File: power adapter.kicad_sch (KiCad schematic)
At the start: 6 parts, among them J1 Conn_02x05_Odd_Even_MountingP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

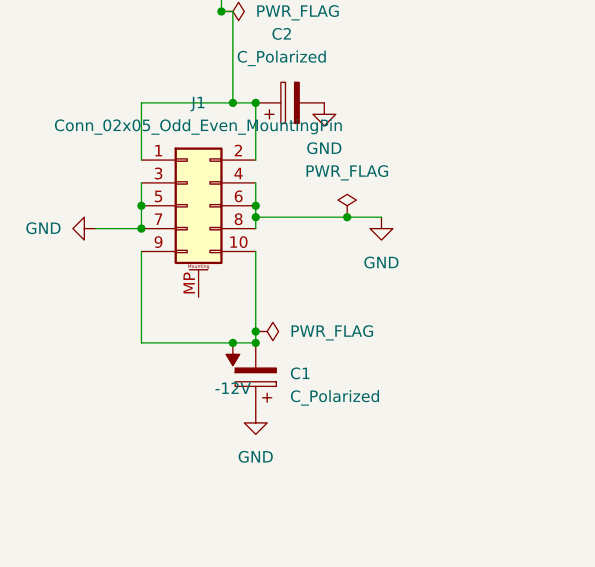
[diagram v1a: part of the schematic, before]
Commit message: added header footprint
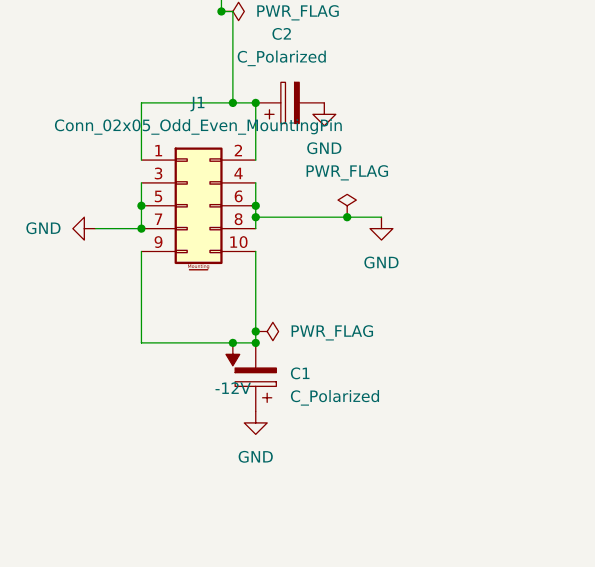
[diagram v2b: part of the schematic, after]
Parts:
- J1: footprint (none) -> Connector_PinHeader_1.00mm:PinHeader_2x05_P1.00mm_Vertical
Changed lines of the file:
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@@
 			)
 		)
-		(property "Footprint" ""
+		(property "Footprint" "Connector_PinHeader_1.00mm:PinHeader_2x05_P1.00mm_Vertical"
 			(at 26.67 48.26 0)
 			(effects
@@
 		(pin "8"
 		)
-		(pin "MP"
-		)
 		(pin "7"

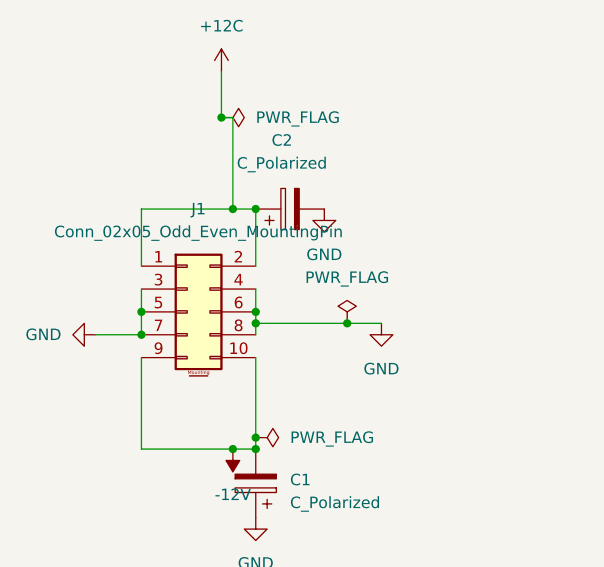
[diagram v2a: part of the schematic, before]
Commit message: fixed header symbol
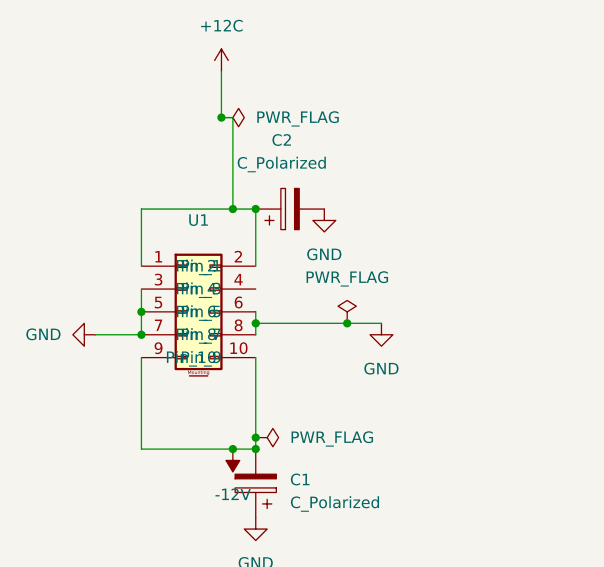
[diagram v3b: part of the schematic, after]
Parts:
- removed J1: Conn_02x05_Odd_Even_MountingPin, Connector_PinHeader_1.00mm:PinHeader_2x05_P1.00mm_Vertical, symbol Connector_Generic_MountingPin:Conn_02x05_Odd_Even_MountingPin
- added U1: ~, symbol adapterlib:header2x5
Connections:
- net +12C: now also U1.1 (Pin_1), U1.2 (Pin_2)
- net -12V: now also U1.10 (Pin_10), U1.9 (Pin_9)
- net GND: now also U1.3 (Pin_3), U1.5 (Pin_5), U1.6 (Pin_6), U1.7 (Pin_7), U1.8 (Pin_8)

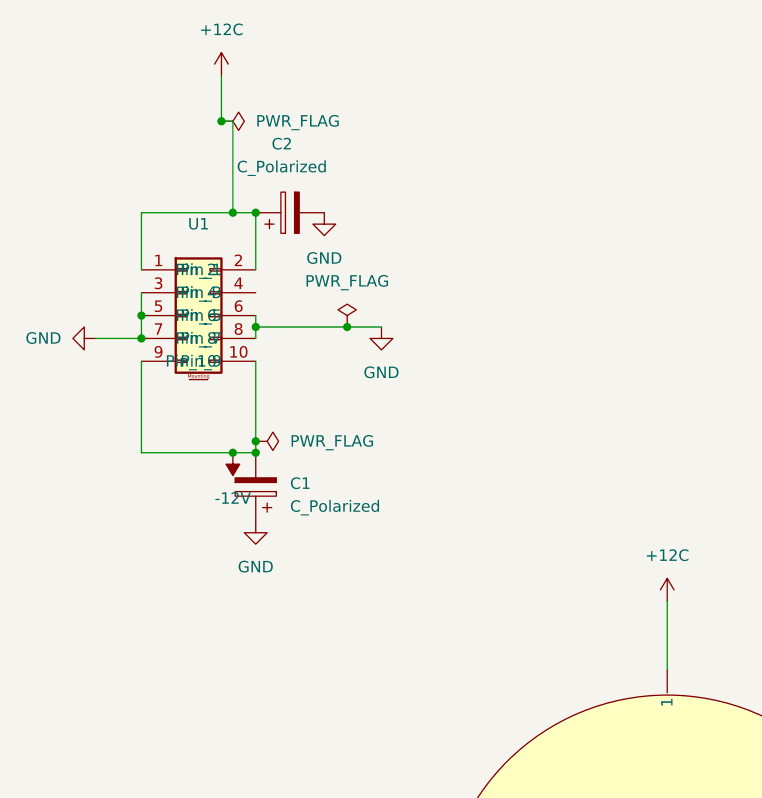
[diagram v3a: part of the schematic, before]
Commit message: added esp32lib to project
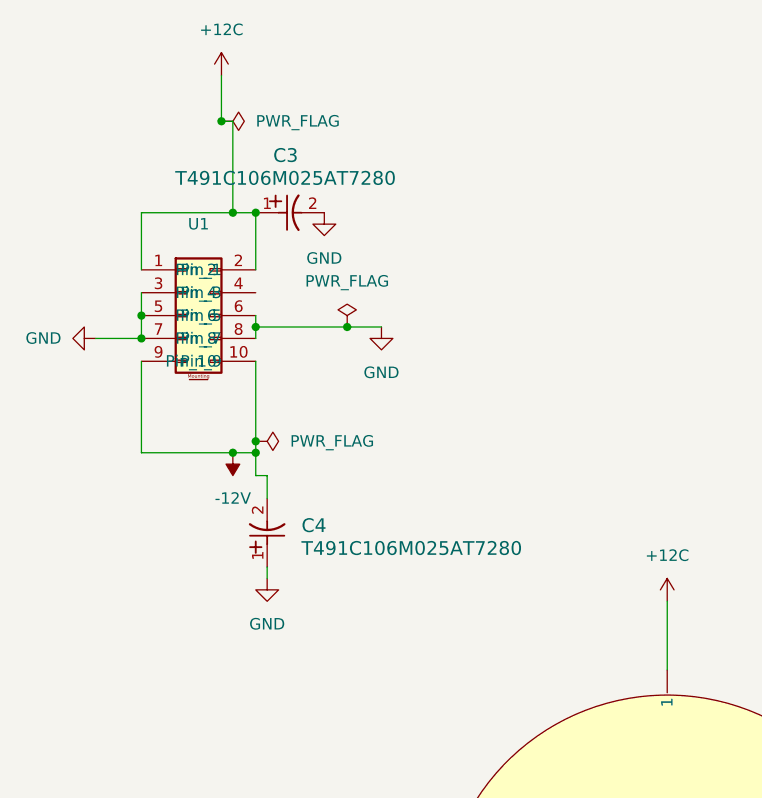
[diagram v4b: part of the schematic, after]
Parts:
- removed C1, C2: C_Polarized, symbol Device:C_Polarized
- added C3, C4: T491C106M025AT7280, customfootprints:10uFtantcap, symbol esp32lib:T491C106M025AT7280
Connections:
- net +12C: now also C3.1
- net -12V: now also C4.2
- net GND: now also C3.2, C4.1
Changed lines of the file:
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@@
 	(paper "A4")
+	(junction
+		(at 44.45 49.53)
+		(diameter 0)
+		(color 0 0 0 0)
+	)
+	(junction
+		(at 21.59 48.26)
+		(diameter 0)
+		(color 0 0 0 0)
+	)
+	(junction
+		(at 30.48 26.67)
+		(diameter 0)
+		(color 0 0 0 0)
+	)
 	(junction
 		(at 34.29 36.83)
@@
 	)
 	(junction
-		(at 44.45 49.53)
-		(diameter 0)
-		(color 0 0 0 0)
-	)
-	(junction
-		(at 21.59 48.26)
-		(diameter 0)
-		(color 0 0 0 0)
-	)
-	(junction
-		(at 30.48 26.67)
-		(diameter 0)
-		(color 0 0 0 0)
-	)
-	(junction
 		(at 21.59 50.8)
 		(diameter 0)
@@
 	)
 	(junction
-		(at 34.29 63.5)
-		(diameter 0)
-		(color 0 0 0 0)
-	)
-	(junction
 		(at 34.29 62.23)
 		(diameter 0)
@@
 	)
 	(junction
+		(at 34.29 63.5)
+		(diameter 0)
+		(color 0 0 0 0)
+	)
+	(junction
 		(at 31.75 63.5)
 		(diameter 0)
@@
 	(wire
 		(pts
+			(xy 34.29 66.04) (xy 34.29 63.5)
+		)
+		(stroke
+			(width 0)
+			(type default)
+		)
+	)
+	(wire
+		(pts
 			(xy 21.59 43.18) (xy 21.59 36.83)
 		)
@@
 	(wire
 		(pts
+			(xy 35.56 77.47) (xy 35.56 76.2)
+		)
+		(stroke
+			(width 0)
+			(type default)
+		)
+	)
+	(wire
+		(pts
 			(xy 34.29 49.53) (xy 34.29 50.8)
 		)
@@
 	(wire
 		(pts
+			(xy 35.56 68.58) (xy 35.56 66.04)
+		)
+		(stroke
+			(width 0)
+			(type default)
+		)
+	)
+	(wire
+		(pts
 			(xy 34.29 48.26) (xy 34.29 49.53)
 		)
@@
 		(pts
 			(xy 140.97 143.51) (xy 148.59 143.51)
+		)
+		(stroke
+			(width 0)
+			(type default)
+		)
+	)
+	(wire
+		(pts
+			(xy 35.56 66.04) (xy 34.29 66.04)
 		)
 		(stroke
@@
 	)
 	(symbol
-		(lib_id "Device:C_Polarized")
-		(at 34.29 67.31 180)
-		(unit 1)
-		(exclude_from_sim no)
-		(in_bom yes)
-		(on_board yes)
-		(dnp no)
-		(fields_autoplaced yes)
-		(property "Reference" "C1"
-			(at 38.1 66.9289 0)
-			(effects
-				(font
-					(size 1.27 1.27)
+		(lib_id "esp32lib:T491C106M025AT7280")
+		(at 35.56 76.2 90)
+		(unit 1)
+		(exclude_from_sim no)
+		(in_bom yes)
+		(on_board yes)
+		(dnp no)
+		(fields_autoplaced yes)
+		(property "Reference" "C4"
+			(at 39.37 71.6025 90)
+			(effects
+				(font
+					(size 1.524 1.524)
 				)
 				(justify right)
 			)
 		)
-		(property "Value" "C_Polarized"
-			(at 38.1 69.4689 0)
-			(effects
-				(font
-					(size 1.27 1.27)
+		(property "Value" "T491C106M025AT7280"
+			(at 39.37 74.1425 90)
+			(effects
+				(font
+					(size 1.524 1.524)
 				)
 				(justify right)
 			)
 		)
-		(property "Footprint" ""
-			(at 33.3248 63.5 0)
-			(effects
-				(font
-					(size 1.27 1.27)
-				)
-				(hide yes)
-			)
-		)
-		(property "Datasheet" "~"
-			(at 34.29 67.31 0)
-			(effects
-				(font
-					(size 1.27 1.27)
-				)
-				(hide yes)
-			)
-		)
-		(property "Description" "Polarized capacitor"
-			(at 34.29 67.31 0)
-			(effects
-				(font
-					(size 1.27 1.27)
-				)
-				(hide yes)
-			)
+		(property "Footprint" "customfootprints:10uFtantcap"
+			(at 35.56 76.2 0)
+			(effects
+				(font
+					(size 1.27 1.27)
+					(italic yes)
+				)
+				(hide yes)
+			)
+		)
+		(property "Datasheet" "T491C106M025AT7280"
+			(at 35.56 76.2 0)
+			(effects
+				(font
+					(size 1.27 1.27)
+					(italic yes)
+				)
+				(hide yes)
+			)
+		)
+		(property "Description" ""
+			(at 35.56 76.2 0)
+			(effects
+				(font
+					(size 1.27 1.27)
+				)
+				(hide yes)
+			)
+		)
+		(pin "2"
 		)
 		(pin "1"
 		)
-		(pin "2"
-		)
-		(instances
-			(project ""
-				(path "/91d95850-e011-4872-8c18-f0f818ae8f1c"
-					(reference "C1")
+		(instances
+			(project ""
+				(path "/91d95850-e011-4872-8c18-f0f818ae8f1c"
+					(reference "C4")
 					(unit 1)
 				)
@@
 	)
 	(symbol
-		(lib_id "Device:C_Polarized")
-		(at 38.1 36.83 90)
-		(unit 1)
-		(exclude_from_sim no)
-		(in_bom yes)
-		(on_board yes)
-		(dnp no)
-		(fields_autoplaced yes)
-		(property "Reference" "C2"
-			(at 37.211 29.21 90)
-			(effects
-				(font
-					(size 1.27 1.27)
-				)
-			)
-		)
-		(property "Value" "C_Polarized"
-			(at 37.211 31.75 90)
-			(effects
-				(font
-					(size 1.27 1.27)
-				)
-			)
-		)
-		(property "Footprint" ""
-			(at 41.91 35.8648 0)
-			(effects
-				(font
-					(size 1.27 1.27)
-				)
-				(hide yes)
-			)
-		)
-		(property "Datasheet" "~"
-			(at 38.1 36.83 0)
-			(effects
-				(font
-					(size 1.27 1.27)
-				)
-				(hide yes)
-			)
-		)
-		(property "Description" "Polarized capacitor"
-			(at 38.1 36.83 0)
-			(effects
-				(font
-					(size 1.27 1.27)
-				)
-				(hide yes)
-			)
-		)
-		(pin "2"
-		)
-		(pin "1"
-		)
-		(instances
-			(project ""
-				(path "/91d95850-e011-4872-8c18-f0f818ae8f1c"
-					(reference "C2")
-					(unit 1)
-				)
-			)
-		)
-	)
-	(symbol
 		(lib_id "power:+12C")
 		(at 30.48 21.59 0)
@@
 	(symbol
 		(lib_id "power:GND")
-		(at 34.29 71.12 0)
+		(at 35.56 77.47 0)
 		(unit 1)
 		(exclude_from_sim no)
@@
 		(fields_autoplaced yes)
 		(property "Reference" "#PWR8"
-			(at 34.29 77.47 0)
+			(at 35.56 83.82 0)
 			(effects
 				(font
@@
 		)
 		(property "Value" "GND"
-			(at 34.29 76.2 0)
+			(at 35.56 82.55 0)
 			(effects
 				(font
@@
 		)
 		(property "Footprint" ""
-			(at 34.29 71.12 0)
+			(at 35.56 77.47 0)
 			(effects
 				(font
@@
 		)
 		(property "Datasheet" ""
-			(at 34.29 71.12 0)
+			(at 35.56 77.47 0)
 			(effects
 				(font
@@
 		)
 		(property "Description" "Power symbol creates a global label with name \"GND\" , ground"
-			(at 34.29 71.12 0)
+			(at 35.56 77.47 0)
 			(effects
 				(font
@@
 					(unit 1)
 				)
+			)
+		)
+	)
+	(symbol
+		(lib_id "esp32lib:T491C106M025AT7280")
+		(at 34.29 36.83 0)
+		(unit 1)
+		(exclude_from_sim no)
+		(in_bom yes)
+		(on_board yes)
+		(dnp no)
+		(fields_autoplaced yes)
+		(property "Reference" "C3"
+			(at 37.6174 30.48 0)
+			(effects
+				(font
+					(size 1.524 1.524)
+				)
+			)
+		)
+		(property "Value" "T491C106M025AT7280"
+			(at 37.6174 33.02 0)
+			(effects
+				(font
+					(size 1.524 1.524)
+				)
+			)
+		)
+		(property "Footprint" "customfootprints:10uFtantcap"
+			(at 34.29 36.83 0)
+			(effects
+				(font
+					(size 1.27 1.27)
+					(italic yes)
+				)
+				(hide yes)
+			)
+		)
+		(property "Datasheet" "T491C106M025AT7280"
+			(at 34.29 36.83 0)
+			(effects
+				(font
+					(size 1.27 1.27)
+					(italic yes)
+				)
+				(hide yes)
+			)
+		)
+		(property "Description" ""
+			(at 34.29 36.83 0)
+			(effects
+				(font
+					(size 1.27 1.27)
+				)
+				(hide yes)
+			)
+		)
+		(pin "1"
+		)
+		(pin "2"
+		)
+		(instances
+			(project ""
+				(path "/91d95850-e011-4872-8c18-f0f818ae8f1c"
+					(reference "C3")
+					(unit 1)
+				)

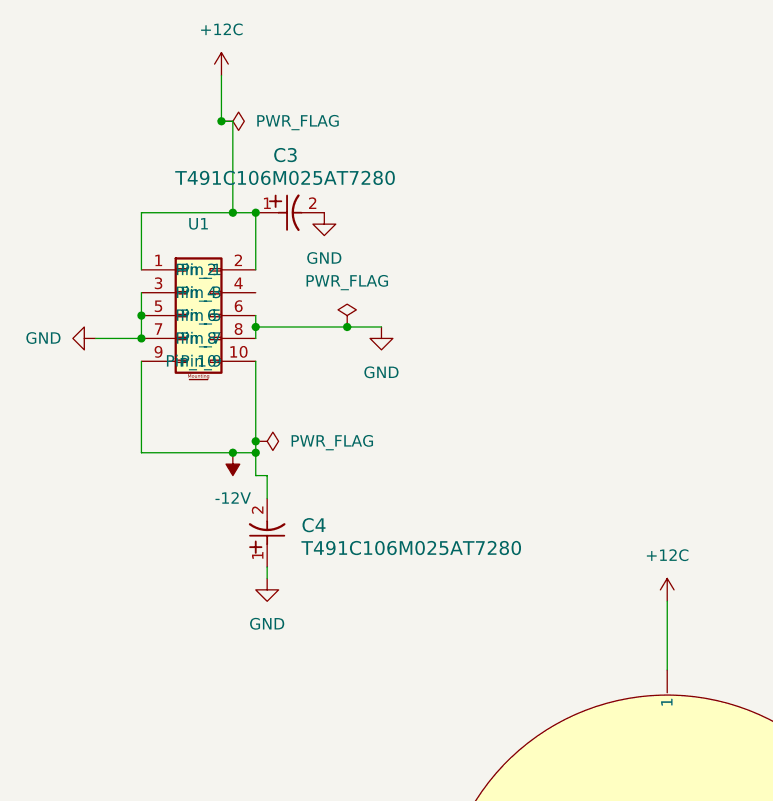
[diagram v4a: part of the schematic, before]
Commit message: header adjusted
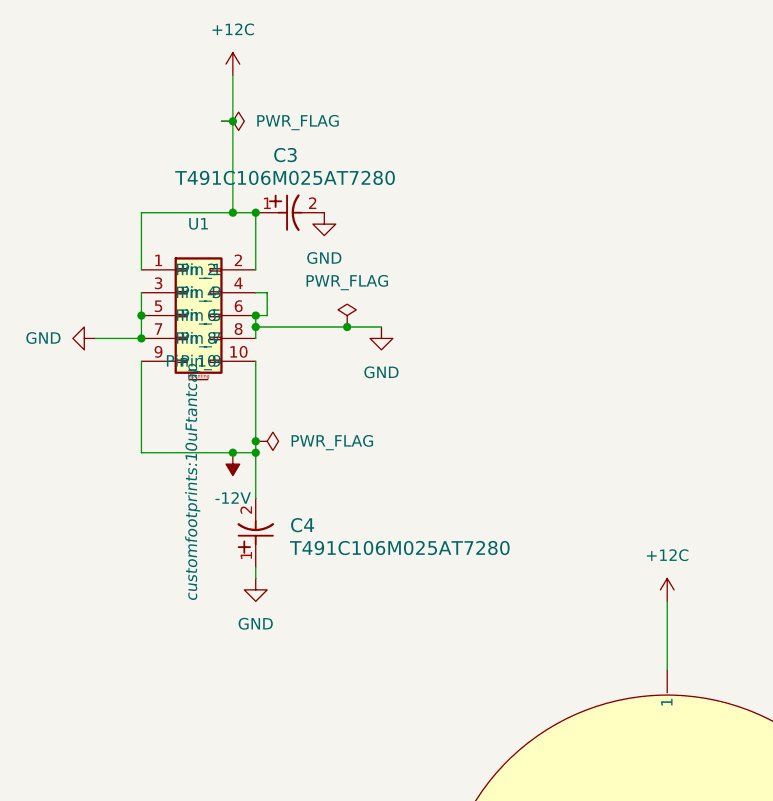
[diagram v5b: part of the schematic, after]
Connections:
- net GND: now also U1.4 (Pin_4)
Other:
- moved on the sheet: C4
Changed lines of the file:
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@@
 	(paper "A4")
+	(junction
+		(at 31.75 26.67)
+		(diameter 0)
+		(color 0 0 0 0)
+	)
 	(junction
 		(at 44.45 49.53)
@@
 	)
 	(junction
-		(at 30.48 26.67)
-		(diameter 0)
-		(color 0 0 0 0)
-	)
-	(junction
 		(at 34.29 36.83)
 		(diameter 0)
@@
 	)
 	(junction
+		(at 34.29 48.26)
+		(diameter 0)
+		(color 0 0 0 0)
+	)
+	(junction
 		(at 31.75 63.5)
 		(diameter 0)
@@
 	(wire
 		(pts
-			(xy 30.48 21.59) (xy 30.48 26.67)
+			(xy 31.75 21.59) (xy 31.75 26.67)
 		)
 		(stroke
@@
 	(wire
 		(pts
+			(xy 35.56 45.72) (xy 35.56 48.26)
+		)
+		(stroke
+			(width 0)
+			(type default)
+		)
+	)
+	(wire
+		(pts
 			(xy 31.75 63.5) (xy 34.29 63.5)
 		)
@@
 	(wire
 		(pts
+			(xy 35.56 45.72) (xy 34.29 45.72)
+		)
+		(stroke
+			(width 0)
+			(type default)
+		)
+	)
+	(wire
+		(pts
 			(xy 34.29 63.5) (xy 34.29 62.23)
 		)
@@
 	(wire
 		(pts
-			(xy 34.29 66.04) (xy 34.29 63.5)
+			(xy 34.29 63.5) (xy 34.29 68.58)
 		)
 		(stroke
@@
 	(wire
 		(pts
-			(xy 35.56 77.47) (xy 35.56 76.2)
+			(xy 34.29 77.47) (xy 34.29 76.2)
 		)
 		(stroke
@@
 	(wire
 		(pts
-			(xy 35.56 68.58) (xy 35.56 66.04)
-		)
-		(stroke
-			(width 0)
-			(type default)
-		)
-	)
-	(wire
-		(pts
 			(xy 34.29 48.26) (xy 34.29 49.53)
 		)
@@
 	(wire
 		(pts
+			(xy 35.56 48.26) (xy 34.29 48.26)
+		)
+		(stroke
+			(width 0)
+			(type default)
+		)
+	)
+	(wire
+		(pts
 			(xy 140.97 143.51) (xy 148.59 143.51)
-		)
-		(stroke
-			(width 0)
-			(type default)
-		)
-	)
-	(wire
-		(pts
-			(xy 35.56 66.04) (xy 34.29 66.04)
 		)
 		(stroke
@@
 	(symbol
 		(lib_id "esp32lib:T491C106M025AT7280")
-		(at 35.56 76.2 90)
+		(at 34.29 76.2 90)
 		(unit 1)
 		(exclude_from_sim no)
@@
 		(fields_autoplaced yes)
 		(property "Reference" "C4"
-			(at 39.37 71.6025 90)
+			(at 38.1 71.6025 90)
 			(effects
 				(font
@@
 		)
 		(property "Value" "T491C106M025AT7280"
-			(at 39.37 74.1425 90)
+			(at 38.1 74.1425 90)
 			(effects
 				(font
@@
 		)
 		(property "Footprint" "customfootprints:10uFtantcap"
-			(at 35.56 76.2 0)
+			(at 27.178 66.802 0)
 			(effects
 				(font
@@
 					(italic yes)
 				)
-				(hide yes)
 			)
 		)
 		(property "Datasheet" "T491C106M025AT7280"
-			(at 35.56 76.2 0)
+			(at 28.702 71.882 0)
 			(effects
 				(font
@@
 		)
 		(property "Description" ""
-			(at 35.56 76.2 0)
+			(at 34.29 76.2 0)
 			(effects
 				(font
@@
 	(symbol
 		(lib_id "power:+12C")
-		(at 30.48 21.59 0)
+		(at 31.75 21.59 0)
 		(unit 1)
 		(exclude_from_sim no)
@@
 		(fields_autoplaced yes)
 		(property "Reference" "#PWR4"
-			(at 30.48 25.4 0)
+			(at 31.75 25.4 0)
 			(effects
 				(font
@@
 		)
 		(property "Value" "+12C"
-			(at 30.48 16.51 0)
+			(at 31.75 16.51 0)
 			(effects
 				(font
@@
 		)
 		(property "Footprint" ""
-			(at 30.48 21.59 0)
+			(at 31.75 21.59 0)
 			(effects
 				(font
@@
 		)
 		(property "Datasheet" ""
-			(at 30.48 21.59 0)
+			(at 31.75 21.59 0)
 			(effects
 				(font
@@
 		)
 		(property "Description" "Power symbol creates a global label with name \"+12C\""
-			(at 30.48 21.59 0)
+			(at 31.75 21.59 0)
 			(effects
 				(font
@@
 	(symbol
 		(lib_id "power:GND")
-		(at 35.56 77.47 0)
+		(at 34.29 77.47 0)
 		(unit 1)
 		(exclude_from_sim no)
@@
 		(fields_autoplaced yes)
 		(property "Reference" "#PWR8"
-			(at 35.56 83.82 0)
+			(at 34.29 83.82 0)
 			(effects
 				(font
@@
 		)
 		(property "Value" "GND"
-			(at 35.56 82.55 0)
+			(at 34.29 82.55 0)
 			(effects
 				(font
@@
 		)
 		(property "Footprint" ""
-			(at 35.56 77.47 0)
+			(at 34.29 77.47 0)
 			(effects
 				(font
@@
 		)
 		(property "Datasheet" ""
-			(at 35.56 77.47 0)
+			(at 34.29 77.47 0)
 			(effects
 				(font
@@
 		)
 		(property "Description" "Power symbol creates a global label with name \"GND\" , ground"
-			(at 35.56 77.47 0)
+			(at 34.29 77.47 0)
 			(effects
 				(font
@@
 		)
 		(property "Footprint" "customfootprints:10uFtantcap"
-			(at 34.29 36.83 0)
+			(at 35.052 40.64 0)
 			(effects
 				(font
@@
 		)
 		(property "Datasheet" "T491C106M025AT7280"
-			(at 34.29 36.83 0)
-			(effects
-				(font
+			(at 34.798 41.402 0)
+			(effects
+				(font

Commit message: board started
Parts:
- U1: footprint (none) -> adapterpcblib:Header2x5
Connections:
- net -12V: now also jk1.2; no longer jk2. (1)
- net GND: now also jk3.2; no longer jk3. (1)
- net +12C renamed +12V
- net +12V: now also jk2.2; no longer jk1. (1)
